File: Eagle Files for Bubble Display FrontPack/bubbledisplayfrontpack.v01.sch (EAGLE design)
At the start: 17 parts, among them CN1 1X4-CLEANBIG

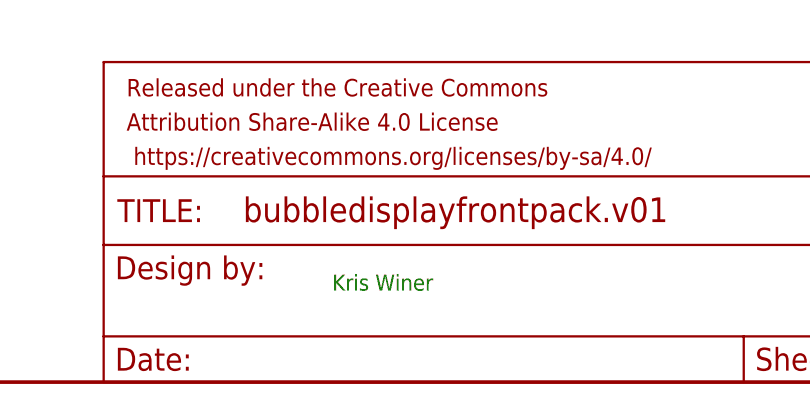
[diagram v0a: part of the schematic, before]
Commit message: BubbleDisplayFrontPackDesign.v01
HT16K33 RAM Mapping 16*8 LED Driver with 4 four-digit, eight-segment
QDSP-6064 bubble displays in a "frontpack" board design
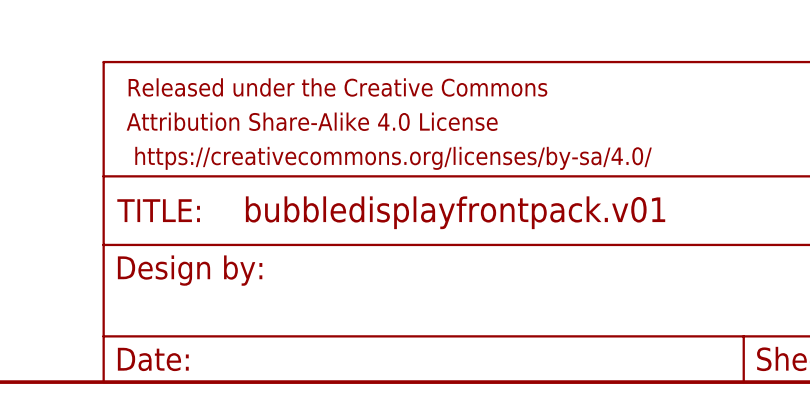
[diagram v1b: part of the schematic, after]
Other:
- note removed: "Kris Winer"
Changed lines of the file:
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@@
 <sheet>
 <plain>
-<text x="337.82" y="-66.04" size="1.778" layer="91">Kris Winer</text>
 </plain>
 <instances>
